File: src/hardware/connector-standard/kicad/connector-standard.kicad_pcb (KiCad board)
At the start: 2 copper layers, 29 x 12 mm, 2 parts, among them J1 ESC Connector, J2 UART Connector

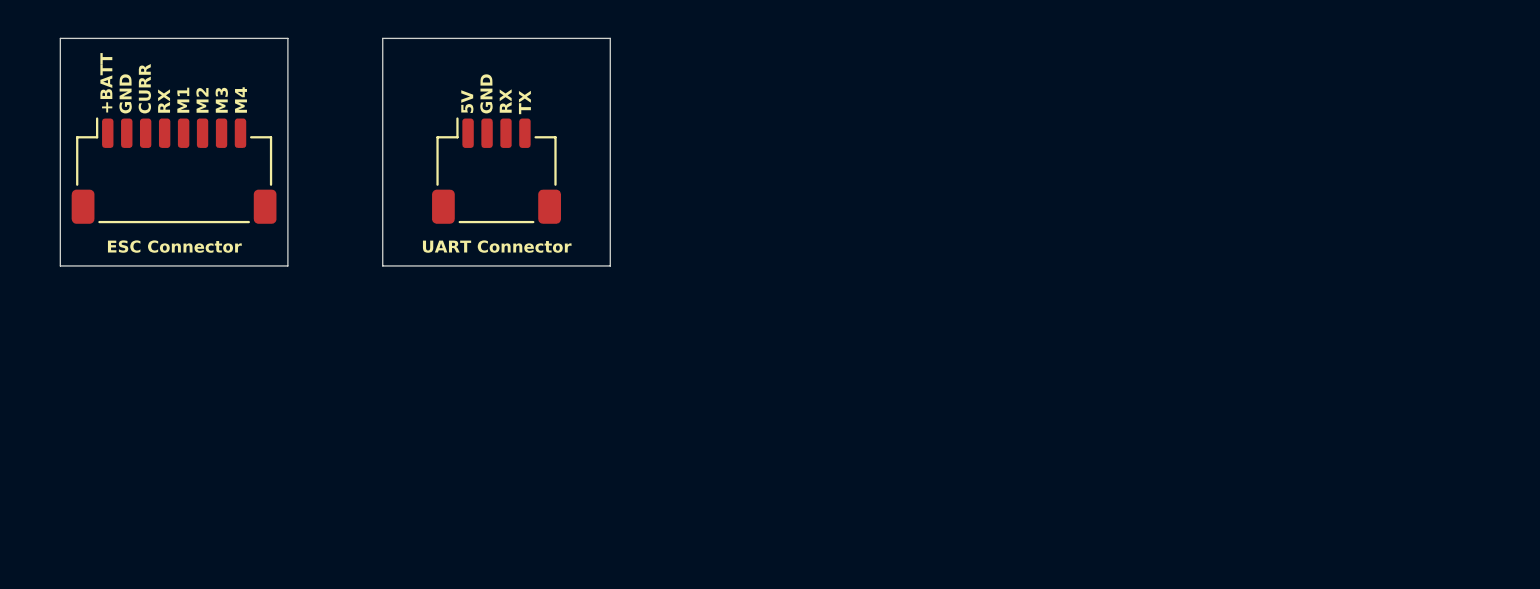
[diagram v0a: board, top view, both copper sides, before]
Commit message: Hardware: Re-implement all existing connectors
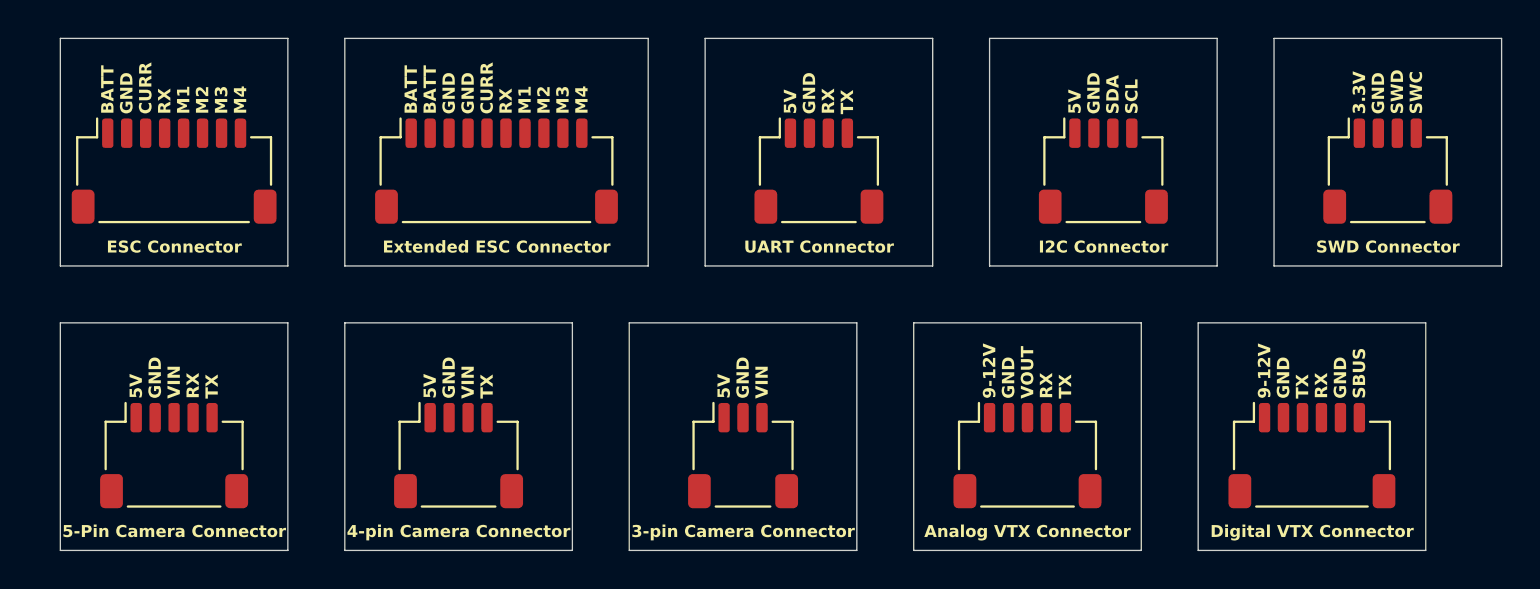
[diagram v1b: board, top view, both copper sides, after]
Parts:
- added J10: Digital VTX Connector, Connector_JST:JST_SH_SM06B-SRSS-TB_1x06-1MP_P1.00mm_Horizontal, F.Cu at (167.0, 123.0)
- added J3: UART Connector, Connector_JST:JST_SH_SM04B-SRSS-TB_1x04-1MP_P1.00mm_Horizontal, F.Cu at (141.0, 108.0)
- added J4: I2C Connector, Connector_JST:JST_SH_SM04B-SRSS-TB_1x04-1MP_P1.00mm_Horizontal, F.Cu at (156.0, 108.0)
- added J5: SWD Connector, Connector_JST:JST_SH_SM04B-SRSS-TB_1x04-1MP_P1.00mm_Horizontal, F.Cu at (171.0, 108.0)
- added J6: 5-pin Camera Connector, Connector_JST:JST_SH_SM05B-SRSS-TB_1x05-1MP_P1.00mm_Horizontal, F.Cu at (107.0, 123.0)
- added J7: 4-pin Camera Connector, Connector_JST:JST_SH_SM04B-SRSS-TB_1x04-1MP_P1.00mm_Horizontal, F.Cu at (122.0, 123.0)
- added J8: 3-pin Camera Connector, Connector_JST:JST_SH_SM03B-SRSS-TB_1x03-1MP_P1.00mm_Horizontal, F.Cu at (137.0, 123.0)
- added J9: Analog VTX Connector, Connector_JST:JST_SH_SM05B-SRSS-TB_1x05-1MP_P1.00mm_Horizontal, F.Cu at (152.0, 123.0)
- J2: value UART Connector -> Extended ESC Connector; footprint Connector_JST:JST_SH_SM04B-SRSS-TB_1x04-1MP_P1.00mm_Horizontal -> Connector_JST:JST_SH_SM10B-SRSS-TB_1x10-1MP_P1.00mm_Horizontal
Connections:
- J2 pad 1: +5V -> +BATT
- J2 pad 2: GND -> +BATT
- J2 pad 3: UART_RX -> GND
- J2 pad 4: UART_TX -> GND
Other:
- board size 29 x 12 mm -> 76 x 27 mm
- board text added: "3-pin Camera Connector"
- board text added: "3.3V"
- board text added: "4-pin Camera Connector"
- board text added: "5-Pin Camera Connector"
- board text added: "5V"
- board text added: "9-12V"
- board text added: "Analog VTX Connector"
- board text added: "BATT"
- board text added: "CURR"
- board text added: "Digital VTX Connector"
- board text added: "Extended ESC Connector"
- board text added: "GND"
- board text added: "I2C Connector"
- board text added: "M1"
- board text added: "M2"
- board text added: "M3"
- board text added: "M4"
- board text added: "RX"
- board text added: "SBUS"
- board text added: "SCL"
- board text added: "SDA"
- board text added: "SWC"
- board text added: "SWD"
- board text added: "SWD Connector"
- board text added: "TX"
- board text added: "VIN"
- board text added: "VOUT"
- board text removed: "+BATT GND CURR RX M1 M2 M3 M4"
- board text removed: "5V GND RX TX"
